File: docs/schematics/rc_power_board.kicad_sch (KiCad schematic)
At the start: 44 parts, among them J1 XT60 battery (gender TBD), J10 Radar, J11 Spare 5V, J12 IMU, J13 Shaft encoder, J14 Spare 3.3V, J2 ESC power (XT60 TBD), J3 ESC Rx lead (BEC in), J4 Servo DS3225MG, J5 Actuator signals to ESP32, J6 Raspberry Pi 5 power, J7 ESP32-S3 5V (left USB), J8 LIDAR-Lite v4, J9 Camera USB hub, U1 Pololu D36V50F5 buck (TBD), U2 5V buck >=4A module, TBD, U3 AP2112K-3.3 (>=300 mA LDO, TB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

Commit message: Fix disconnected power LEDs and review findings in power board baseline
Independent review of ac5b49b found:
- D2-D4 were placed 3.81 mm below their resistors, leaving all three
  power LEDs unconnected (6 single-pin nets). LEDs now sit on R pin 2;
  netlist is 19 nets with Net-(D2-A)/(D3-A)/(D4-A).
- +6V_BEC (local label "/+6V_BEC") fell into the Default net class;
  pattern is now "*+6V_BEC" (Power3A).
- D1 now Device:D_Zener as a unidirectional TVS, cathode to VBAT
  (plan text updated to match).
- U1 value keeps the plan requirement; hidden U3 NC pin no longer gets
  an extra no-connect marker; Notes item 8 lists the real patterns.
- Layout: text overlaps removed, Notes box inside the frame, region E
  clear of the title block.
- README: verification claims corrected (ERC never run), all deviations
  and placeholder footprints listed.

Co-Authored-By: Claude Opus 5.5 <noreply@anthropic.com>
Claude-Session: https://claude.ai/code/session_019hn8SCZUUAVD8H8MEh7Mv7
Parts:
- removed H4: MountingHole_M3, MountingHole:MountingHole_3.2mm_M3, symbol Mechanical:MountingHole
- added H1: MountingHole_M3, MountingHole:MountingHole_3.2mm_M3, symbol Mechanical:MountingHole
- C1: value TBD uF >=16V low-ESR -> TBD uF >=16V
- D1: value TVS TBD, standoff >=9V -> TVS unidir. TBD; symbol Device:D_TVS -> Device:D_Zener
- J2: value ESC power (XT60 TBD) -> ESC power (XT60)
- J7: value ESP32-S3 5V (left USB) -> ESP32-S3 5V
- U1: value Pololu D36V50F5 buck (TBD) -> D36V50F5 buck TBD (req 5.1V >=6A)
- renumbered H1 to H2, H2 to H3, H3 to H4
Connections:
- net at D2.2 (A): now also R1.2
- net at R2.2: now also D3.2 (A)
- net at R3.2: now also D4.2 (A)
- no-connect marks 3 -> 2
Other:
- moved on the sheet: D2, D3, H2, H3, H4, J2, R1, R2

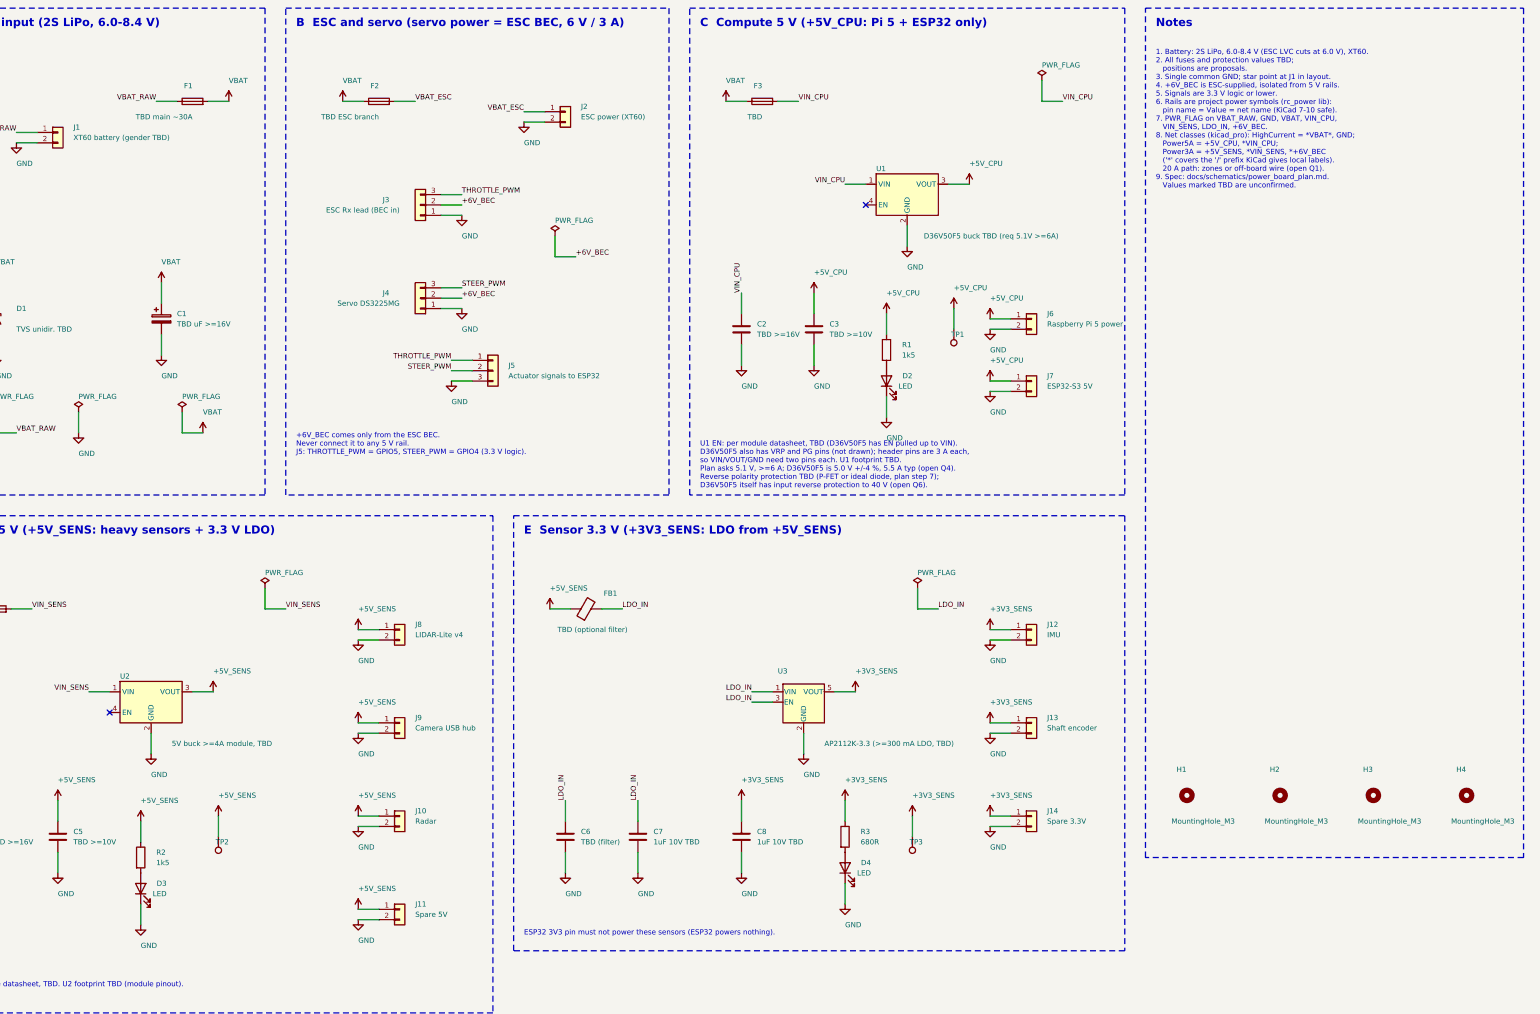
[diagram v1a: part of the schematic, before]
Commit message: Draw full D36V50F5, EN/PG to ESP32, T-plug pads, USB-C pigtails
- U1: Pololu D36V50F5 with all 12 pins (PG, EN, 2x VRP, 2x VIN, 4x GND,
  2x VOUT) on a 2x6 0.1 in footprint; pin pairs joined. VRP unused: the
  sensor buck stays on VBAT via F4.
- EN: never direct to a GPIO (100k pull-up to VIN, up to 8.4 V; U1 also
  powers the ESP32). Proposed shutdown FET Q1 (2N7002) + R4 100k gate
  pull-down on ESP_SHDN; approach left open (open question 13).
- PG (open drain) to the ESP32 via J5, now 5 pins; GPIOs TBD.
- J1/J2: wire pads for 12 AWG T-plug pigtails (pad size TBD).
- J6/J7: 2-wire USB-C pigtails into the Pi 5 and ESP32 USB-C inputs.
- Plan doc re-exported (steps 5-7, footprints, open questions 3/4/6/8/12-14,
  "why the extra parts"); README and schematics rule updated.

Co-Authored-By: Claude Opus 5.5 <noreply@anthropic.com>
Claude-Session: https://claude.ai/code/session_019hn8SCZUUAVD8H8MEh7Mv7
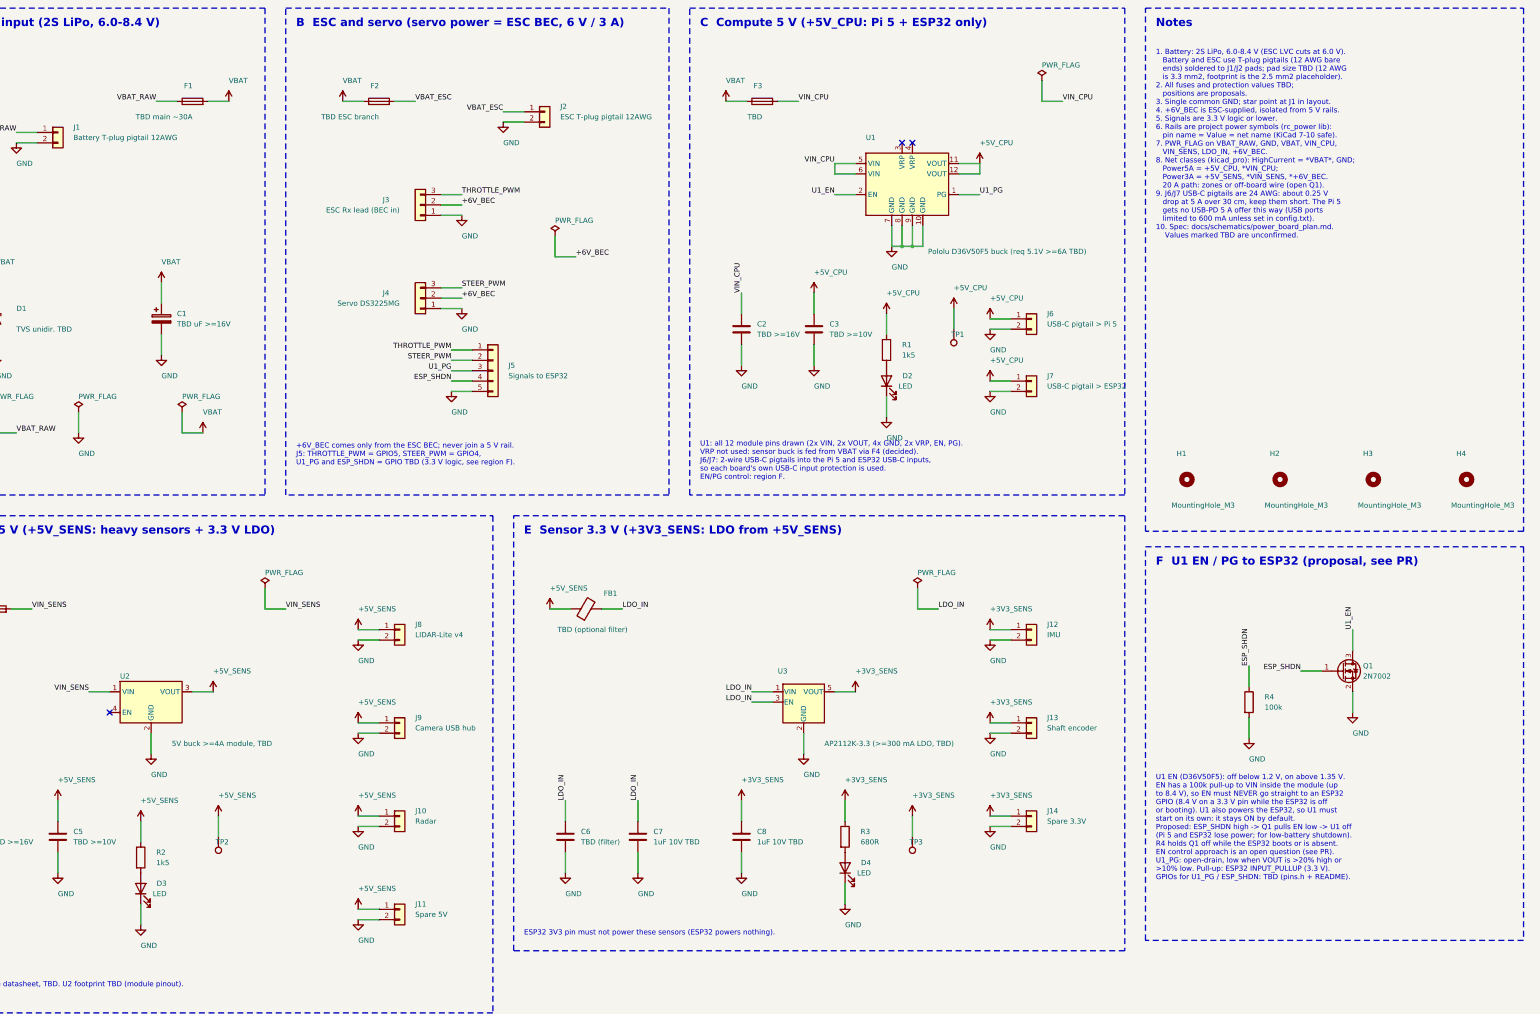
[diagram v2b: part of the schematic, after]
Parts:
- removed C6: TBD (filter), Capacitor_SMD:C_0805_2012Metric, symbol Device:C
- removed J12: IMU, Connector_JST:JST_XH_B2B-XH-A_1x02_P2.50mm_Vertical, symbol Connector_Generic:Conn_01x02
- removed J5: Actuator signals to ESP32, Connector_PinHeader_2.54mm:PinHeader_1x03_P2.54mm_Vertical, symbol Connector_Generic:Conn_01x03
- removed U1: D36V50F5 buck TBD (req 5.1V >=6A), symbol rc_power:REG_MODULE
- added D4: LED, LED_SMD:LED_0805_2012Metric, symbol Device:LED
- added H3: MountingHole_M3, MountingHole:MountingHole_3.2mm_M3, symbol Mechanical:MountingHole
- added J5: Signals to ESP32, Connector_PinHeader_2.54mm:PinHeader_1x05_P2.54mm_Vertical, symbol Connector_Generic:Conn_01x05
- added Q1: 2N7002, Package_TO_SOT_SMD:SOT-23, symbol Transistor_FET:2N7002
- added R4: 100k, Resistor_SMD:R_0805_2012Metric, symbol Device:R
- added U1: Pololu D36V50F5 buck (req 5.1V >=6A TBD), Connector_PinHeader_2.54mm:PinHeader_2x06_P2.54mm_Vertical, symbol rc_power:D36V50F5
- C6: renamed from D4; value LED -> TBD (filter); footprint LED_SMD:LED_0805_2012Metric -> Capacitor_SMD:C_0805_2012Metric; symbol Device:LED -> Device:C
- J1: value XT60 battery (gender TBD) -> Battery T-plug pigtail 12AWG; footprint Connector_AMASS:AMASS_XT60-M_1x02_P7.20mm_Vertical -> Connector_Wire:SolderWire-2.5sqmm_1x02_P8.8mm_D2.4mm_OD4.4mm
- J12: renamed from H3; value MountingHole_M3 -> IMU; footprint MountingHole:MountingHole_3.2mm_M3 -> Connector_JST:JST_XH_B2B-XH-A_1x02_P2.50mm_Vertical; symbol Mechanical:MountingHole -> Connector_Generic:Conn_01x02
- J2: value ESC power (XT60) -> ESC T-plug pigtail 12AWG; footprint Connector_AMASS:AMASS_XT60-M_1x02_P7.20mm_Vertical -> Connector_Wire:SolderWire-2.5sqmm_1x02_P8.8mm_D2.4mm_OD4.4mm
- J6: value Raspberry Pi 5 power -> USB-C pigtail > Pi 5
- J7: value ESP32-S3 5V -> USB-C pigtail > ESP32
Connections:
- net +3V3_SENS: now also J12.1 (Pin_1)
- net +5V_CPU: now also U1.11 (VOUT), U1.12 (VOUT)
- net GND: now also C6.2, J12.2 (Pin_2), D4.1 (K), J5.5 (Pin_5), Q1.2 (S), R4.2, U1.10 (GND), U1.7 (GND), U1.8 (GND), U1.9 (GND); no longer C6.1 (K)
- net LDO_IN: now also C6.1
- net STEER_PWM: now also J5.2 (Pin_2)
- net THROTTLE_PWM: now also J5.1 (Pin_1)
- net VIN_CPU: now also U1.5 (VIN), U1.6 (VIN)
- net at R3.2: now also D4.2 (A); no longer C6.2 (A)
- new net ESP_SHDN: J5.4 (Pin_4), Q1.1 (G), R4.1
- new net U1_EN: Q1.3 (D), U1.2 (EN)
- new net U1_PG: J5.3 (Pin_3), U1.1 (PG)
- no-connect marks 2 -> 3
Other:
- note added: "+6V_BEC comes only from the ESC BEC; never join a 5 V rail. J5: THROTTLE_PWM = GPIO5, STEER_PWM = GPIO4, U1_PG and ESP_SHDN = GPIO TBD (3.3 V logic, see region F)."
- note added: "1. Battery: 2S LiPo, 6.0-8.4 V (ESC LVC cuts at 6.0 V). Battery and ESC use T-plug pigtails (12 AWG bare ends) soldered to J1/J2 pads; pad size TBD (12 AWG is 3.3 mm2, footprint is the 2.5 mm2 placeholder). 2. All fuses and protection values TBD; positions are proposals. 3. Single common GND; star point at J1 in layout. 4. +6V_BEC is ESC-supplied, isolated from 5 V rails. 5. Signals are 3.3 V log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"
- note added: "F U1 EN / PG to ESP32 (proposal, see PR)"
- note added: "U1 EN (D36V50F5): off below 1.2 V, on above 1.35 V. EN has a 100k pull-up to VIN inside the module (up to 8.4 V), so EN must NEVER go straight to an ESP32 GPIO (8.4 V on a 3.3 V pin while the ESP32 is off or booting). U1 also powers the ESP32, so U1 must start on its own: it stays ON by default. Proposed: ESP_SHDN high -> Q1 pulls EN low -> U1 off (Pi 5 and ESP32 lose power; for low-battery shutd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"
- note added: "U1: all 12 module pins drawn (2x VIN, 2x VOUT, 4x GND, 2x VRP, EN, PG). VRP not used: sensor buck is fed from VBAT via F4 (decided). J6/J7: 2-wire USB-C pigtails into the Pi 5 and ESP32 USB-C inputs, so each board's own USB-C input protection is used. EN/PG control: region F."
- note removed: "+6V_BEC comes only from the ESC BEC. Never connect it to any 5 V rail. J5: THROTTLE_PWM = GPIO5, STEER_PWM = GPIO4 (3.3 V logic)."
- note removed: "1. Battery: 2S LiPo, 6.0-8.4 V (ESC LVC cuts at 6.0 V), XT60. 2. All fuses and protection values TBD; positions are proposals. 3. Single common GND; star point at J1 in layout. 4. +6V_BEC is ESC-supplied, isolated from 5 V rails. 5. Signals are 3.3 V logic or lower. 6. Rails are project power symbols (rc_power lib): pin name = Value = net name (KiCad 7-10 safe). 7. PWR_FLAG on VBAT_RAW, GND, VBAT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"
- note removed: "U1 EN: per module datasheet, TBD (D36V50F5 has EN pulled up to VIN). D36V50F5 also has VRP and PG pins (not drawn); header pins are 3 A each, so VIN/VOUT/GND need two pins each. U1 footprint TBD. Plan asks 5.1 V, >=6 A; D36V50F5 is 5.0 V +/-4 %, 5.5 A typ (open Q4). Reverse polarity protection TBD (P-FET or ideal diode, plan step 7); D36V50F5 itself has input reverse protection to 40 V (open Q6)."
- moved on the sheet: J2

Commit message: Address review: EN power-cycle wording, GPIO caution, decoupling caps
- Region F, plan step 7 and open question 13: Q1 power-cycles U1 (U1
  restarts once the ESP32 loses power); it is not a latching shutdown.
  ESP_SHDN / U1_PG must use non-strapping GPIOs, no reset pull-up.
- Plan: C2-C5 explained as decoupling caps, not low-pass filters
  (FB1 + C6 is the LC filter); XT60 leftovers replaced by T-plug;
  six regions; wire-pad hole size corrected.
- Sheet: shorter J6/J7 values, D1 keeps ">=9V", region F title
  references open question 13. README ERC expectations corrected.

Co-Authored-By: Claude Opus 5.5 <noreply@anthropic.com>
Claude-Session: https://claude.ai/code/session_019hn8SCZUUAVD8H8MEh7Mv7
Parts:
- D1: value TVS unidir. TBD -> TVS unidir. >=9V TBD
- J6: value USB-C pigtail > Pi 5 -> USB-C > Pi 5
- J7: value USB-C pigtail > ESP32 -> USB-C > ESP32
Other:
- note added: "F U1 EN / PG to ESP32 (proposal, open Q13)"
- note added: "U1 EN (D36V50F5): off below 1.2 V, on above 1.35 V. EN has a 100k pull-up to VIN inside the module (up to 8.4 V), so EN must NEVER go straight to an ESP32 GPIO (8.4 V on a 3.3 V pin while the ESP32 is off or booting). U1 also powers the ESP32, so U1 must start on its own: it stays ON by default. Proposed: ESP_SHDN high -> Q1 pulls EN low -> U1 off. This is a POWER CYCLE, not a shutdown: the ESP32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"
- note removed: "F U1 EN / PG to ESP32 (proposal, see PR)"
- note removed: "U1 EN (D36V50F5): off below 1.2 V, on above 1.35 V. EN has a 100k pull-up to VIN inside the module (up to 8.4 V), so EN must NEVER go straight to an ESP32 GPIO (8.4 V on a 3.3 V pin while the ESP32 is off or booting). U1 also powers the ESP32, so U1 must start on its own: it stays ON by default. Proposed: ESP_SHDN high -> Q1 pulls EN low -> U1 off (Pi 5 and ESP32 lose power; for low-battery shutd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"
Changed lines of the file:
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@@
     (in_bom yes) (on_board yes) (dnp no)
     (property "Reference" "D1" (at 35.56 93.98 90) (effects (font (size 1.27 1.27)) (justify left)))
-    (property "Value" "TVS unidir. TBD" (at 35.56 99.06 90) (effects (font (size 1.27 1.27)) (justify left)))
+    (property "Value" "TVS unidir. >=9V TBD" (at 35.56 99.06 90) (effects (font (size 1.27 1.27)) (justify left)))
     (property "Footprint" "Diode_SMD:D_SMB" (at 30.48 96.52 0) (effects (font (size 1.27 1.27)) hide))
     (property "Datasheet" "" (at 30.48 96.52 0) (effects (font (size 1.27 1.27)) hide))
@@
     (in_bom yes) (on_board yes) (dnp no)
     (property "Reference" "J6" (at 288.29 95.25 0) (effects (font (size 1.27 1.27)) (justify left)))
-    (property "Value" "USB-C pigtail > Pi 5" (at 288.29 97.78999999999999 0) (effects (font (size 1.27 1.27)) (justify left)))
+    (property "Value" "USB-C > Pi 5" (at 288.29 97.78999999999999 0) (effects (font (size 1.27 1.27)) (justify left)))
     (property "Footprint" "TerminalBlock_Phoenix:TerminalBlock_Phoenix_MKDS-1,5-2-5.08_1x02_P5.08mm_Horizontal" (at 284.48 96.52 0) (effects (font (size 1.27 1.27)) hide))
     (property "Datasheet" "" (at 284.48 96.52 0) (effects (font (size 1.27 1.27)) hide))
@@
     (in_bom yes) (on_board yes) (dnp no)
     (property "Reference" "J7" (at 288.29 110.49000000000001 0) (effects (font (size 1.27 1.27)) (justify left)))
-    (property "Value" "USB-C pigtail > ESP32" (at 288.29 113.03 0) (effects (font (size 1.27 1.27)) (justify left)))
+    (property "Value" "USB-C > ESP32" (at 288.29 113.03 0) (effects (font (size 1.27 1.27)) (justify left)))
     (property "Footprint" "TerminalBlock_Phoenix:TerminalBlock_Phoenix_MKDS-1,5-2-5.08_1x02_P5.08mm_Horizontal" (at 284.48 111.76 0) (effects (font (size 1.27 1.27)) hide))
     (property "Datasheet" "" (at 284.48 111.76 0) (effects (font (size 1.27 1.27)) hide))
@@
     (instances (project "rc_power_board" (path "/6f1c2a52-6a43-4c1e-9a3e-5b0d9c2e7a11" (reference "H4") (unit 1)))))
   (rectangle (start 312.42 152.4) (end 405.13 248.92) (stroke (width 0) (type dash)) (fill (type none)))
-  (text "F  U1 EN / PG to ESP32 (proposal, see PR)" (at 314.96000000000004 154.94 0) (effects (font (size 2.0 2.0) bold) (justify left top)))
+  (text "F  U1 EN / PG to ESP32 (proposal, open Q13)" (at 314.96000000000004 154.94 0) (effects (font (size 2.0 2.0) bold) (justify left top)))
   (symbol (lib_id "Transistor_FET:2N7002") (at 360.68 182.88 0) (unit 1)
     (in_bom yes) (on_board yes) (dnp no)
@@
     (pin "1")
     (instances (project "rc_power_board" (path "/6f1c2a52-6a43-4c1e-9a3e-5b0d9c2e7a11" (reference "#PWR068") (unit 1)))))
-  (text "U1 EN (D36V50F5): off below 1.2 V, on above 1.35 V.\nEN has a 100k pull-up to VIN inside the module (up\nto 8.4 V), so EN must NEVER go straight to an ESP32\nGPIO (8.4 V on a 3.3 V pin while the ESP32 is off\nor booting). U1 also powers the ESP32, so U1 must\nstart on its own: it stays ON by default.\nProposed: ESP_SHDN high -> Q1 pulls EN low -> U1 off\n(Pi 5 and ESP32 lose power; for low-battery shutdown).\nR4 holds Q1 off while the ESP32 boots or is absent.\nEN control approach is an open question (see PR).\nU1_PG: open-drain, low when VOUT is >20% high or\n>10% low. Pull-up: ESP32 INPUT_PULLUP (3.3 V).\nGPIOs for U1_PG / ESP_SHDN: TBD (pins.h + README)." (at 314.96 208.28 0) (effects (font (size 1.27 1.27)) (justify left top)))
+  (text "U1 EN (D36V50F5): off below 1.2 V, on above 1.35 V.\nEN has a 100k pull-up to VIN inside the module (up\nto 8.4 V), so EN must NEVER go straight to an ESP32\nGPIO (8.4 V on a 3.3 V pin while the ESP32 is off\nor booting). U1 also powers the ESP32, so U1 must\nstart on its own: it stays ON by default.\nProposed: ESP_SHDN high -> Q1 pulls EN low -> U1 off.\nThis is a POWER CYCLE, not a shutdown: the ESP32 loses\npower, R4 turns Q1 off, U1 restarts and the Pi 5 and\nESP32 reboot (hard cut to the Pi). A true low-battery\ncutoff needs a latch or a VIN divider on EN (open Q13).\nR4 holds Q1 off while the ESP32 boots or is absent.\nESP_SHDN: non-strapping GPIO, no pull-up at reset.\nU1_PG: non-strapping GPIO (PG is low while VOUT ramps).\nU1_PG: open-drain, low when VOUT is >20% high or\n>10% low. Pull-up: ESP32 INPUT_PULLUP (3.3 V).\nGPIOs for U1_PG / ESP_SHDN: TBD (pins.h + README)." (at 314.96 208.28 0) (effects (font (size 1.27 1.27)) (justify left top)))
   (sheet_instances
     (path "/" (page "1"))
